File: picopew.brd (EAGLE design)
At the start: 48.4 x 20 mm, 16 parts, among them U1 IS31FL3733-TQLS4

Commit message: Silkscreen labeling and decorations.
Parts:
- added U$1: (no value), cwlogo:PICOPEW-O
- added U$10: (no value), cwtypeset:CHAR079
- added U$11: (no value), cwtypeset:CHAR078
- added U$12: (no value), cwlogo:MINUS
- added U$14, U$20, U$22: (no value), cwtypeset:CHAR082
- added U$15, U$21: (no value), cwtypeset:CHAR050
- added U$16: (no value), cwtypeset:CHAR048
- added U$17, U$19, U$25, U$26, U$9: (no value), cwtypeset:CHAR049
- added U$18, U$31: (no value), cwtypeset:CHAR057
- added U$2: (no value), cwlogo:PICOPEW-CORNER-L
- added U$23, U$29: (no value), cwtypeset:CHAR051
- added U$24: (no value), cwtypeset:CHAR067
- added U$27, U$30: (no value), cwtypeset:CHAR054
- added U$28: (no value), cwtypeset:CHAR055
- added U$3: (no value), cwlogo:PICOPEW-X
- added U$4: (no value), cwlogo:PLUS
- added U$5: (no value), cwlogo:PICOPEW
- added U$52, U$59: (no value), cwtypeset:CHAR104
- added U$53, U$54, U$77: (no value), cwtypeset:CHAR116
- added U$55, U$71: (no value), cwtypeset:CHAR112
- added U$56: (no value), cwtypeset:CHAR058
- added U$57, U$58, U$70, U$78: (no value), cwtypeset:CHAR047
- added U$6, U$72: (no value), cwtypeset:CHAR114
- added U$60, U$63, U$65: (no value), cwtypeset:CHAR097
- added U$61, U$76: (no value), cwtypeset:CHAR099
- added U$62: (no value), cwtypeset:CHAR107
- added U$64: (no value), cwtypeset:CHAR100
- added U$66: (no value), cwtypeset:CHAR121
- added U$67: (no value), cwtypeset:CHAR046
- added U$68: (no value), cwtypeset:CHAR105
- added U$69, U$73: (no value), cwtypeset:CHAR111
- added U$7: (no value), cwlogo:CWLOGO-4
- added U$74: (no value), cwtypeset:CHAR106
- added U$75: (no value), cwtypeset:CHAR101
- added U$8: (no value), cwlogo:PICOPEW-CORNER-R
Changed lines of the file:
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@@
 <element name="4" library="cwpackage" package="SINGLEPAD" value="SINGLEPAD" x="8" y="13.81"/>
 <element name="5" library="cwpackage" package="SINGLEPAD" value="SINGLEPAD" x="8" y="6.19"/>
+<element name="U$5" library="cwlogo" package="PICOPEW" value="" x="15.4" y="13.6" rot="R330"/>
+<element name="U$7" library="cwlogo" package="CWLOGO-4" value="" x="16.4" y="5.6" rot="R330"/>
+<element name="U$2" library="cwlogo" package="PICOPEW-CORNER-L" value="" x="2.4" y="0"/>
+<element name="U$8" library="cwlogo" package="PICOPEW-CORNER-R" value="" x="50.8" y="0"/>
+<element name="U$15" library="cwtypeset" package="CHAR050" value="" x="5.545896875" y="2.3" rot="R330"/>
+<element name="U$16" library="cwtypeset" package="CHAR048" value="" x="6.20840625" y="1.917503125" rot="R330"/>
+<element name="U$17" library="cwtypeset" package="CHAR049" value="" x="6.870915625" y="1.535003125" rot="R330"/>
+<element name="U$18" library="cwtypeset" package="CHAR057" value="" x="7.533425" y="1.152503125" rot="R330"/>
+<element name="U$6" library="cwtypeset" package="CHAR114" value="" x="12.941153125" y="12.92320625" rot="R330"/>
+<element name="U$9" library="cwtypeset" package="CHAR049" value="" x="13.382825" y="12.66820625" rot="R330"/>
+<element name="U$10" library="cwtypeset" package="CHAR079" value="" x="2.76435625" y="16.842821875" rot="R330"/>
+<element name="U$11" library="cwtypeset" package="CHAR078" value="" x="3.6373125" y="16.338821875" rot="R330"/>
+<element name="U$14" library="cwtypeset" package="CHAR082" value="" x="45.75" y="18.45" rot="MR270"/>
+<element name="U$19" library="cwtypeset" package="CHAR049" value="" x="45.75" y="17.625" rot="MR270"/>
+<element name="U$20" library="cwtypeset" package="CHAR082" value="" x="25.24" y="9.65"/>
+<element name="U$21" library="cwtypeset" package="CHAR050" value="" x="26.065" y="9.65"/>
+<element name="U$22" library="cwtypeset" package="CHAR082" value="" x="23.03" y="9.65"/>
+<element name="U$23" library="cwtypeset" package="CHAR051" value="" x="23.855" y="9.65"/>
+<element name="U$24" library="cwtypeset" package="CHAR067" value="" x="32.22" y="6.8"/>
+<element name="U$25" library="cwtypeset" package="CHAR049" value="" x="33.059" y="6.8"/>
+<element name="U$1" library="cwlogo" package="PICOPEW-O" value="" x="44.59" y="16.21" rot="R30"/>
+<element name="U$3" library="cwlogo" package="PICOPEW-X" value="" x="42.05" y="8.59" rot="R30"/>
+<element name="U$52" library="cwtypeset" package="CHAR104" value="" x="18.2" y="15.85" rot="MR270"/>
+<element name="U$53" library="cwtypeset" package="CHAR116" value="" x="18.2" y="15.036" rot="MR270"/>
+<element name="U$54" library="cwtypeset" package="CHAR116" value="" x="18.2" y="14.546" rot="MR270"/>
+<element name="U$55" library="cwtypeset" package="CHAR112" value="" x="18.2" y="14.056" rot="MR270"/>
+<element name="U$56" library="cwtypeset" package="CHAR058" value="" x="18.2" y="13.225" rot="MR270"/>
+<element name="U$57" library="cwtypeset" package="CHAR047" value="" x="18.2" y="12.894" rot="MR270"/>
+<element name="U$58" library="cwtypeset" package="CHAR047" value="" x="18.2" y="12.459" rot="MR270"/>
+<element name="U$59" library="cwtypeset" package="CHAR104" value="" x="18.2" y="12.024" rot="MR270"/>
+<element name="U$60" library="cwtypeset" package="CHAR097" value="" x="18.2" y="11.21" rot="MR270"/>
+<element name="U$61" library="cwtypeset" package="CHAR099" value="" x="18.2" y="10.483" rot="MR270"/>
+<element name="U$62" library="cwtypeset" package="CHAR107" value="" x="18.2" y="9.869" rot="MR270"/>
+<element name="U$63" library="cwtypeset" package="CHAR097" value="" x="18.2" y="9.119" rot="MR270"/>
+<element name="U$64" library="cwtypeset" package="CHAR100" value="" x="18.2" y="8.392" rot="MR270"/>
+<element name="U$65" library="cwtypeset" package="CHAR097" value="" x="18.2" y="7.564" rot="MR270"/>
+<element name="U$66" library="cwtypeset" package="CHAR121" value="" x="18.2" y="6.837" rot="MR270"/>
+<element name="U$67" library="cwtypeset" package="CHAR046" value="" x="18.2" y="6.116" rot="MR270"/>
+<element name="U$68" library="cwtypeset" package="CHAR105" value="" x="18.2" y="5.785" rot="MR270"/>
+<element name="U$69" library="cwtypeset" package="CHAR111" value="" x="18.2" y="5.434" rot="MR270"/>
+<element name="U$70" library="cwtypeset" package="CHAR047" value="" x="18.2" y="4.635" rot="MR270"/>
+<element name="U$71" library="cwtypeset" package="CHAR112" value="" x="20" y="14.7" rot="MR270"/>
+<element name="U$72" library="cwtypeset" package="CHAR114" value="" x="20" y="13.869" rot="MR270"/>
+<element name="U$73" library="cwtypeset" package="CHAR111" value="" x="20" y="13.359" rot="MR270"/>
+<element name="U$74" library="cwtypeset" package="CHAR106" value="" x="20" y="12.56" rot="MR270"/>
+<element name="U$75" library="cwtypeset" package="CHAR101" value="" x="20" y="12.183" rot="MR270"/>
+<element name="U$76" library="cwtypeset" package="CHAR099" value="" x="20" y="11.456" rot="MR270"/>
+<element name="U$77" library="cwtypeset" package="CHAR116" value="" x="20" y="10.842" rot="MR270"/>
+<element name="U$78" library="cwtypeset" package="CHAR047" value="" x="20" y="10.352" rot="MR270"/>
+<element name="U$26" library="cwtypeset" package="CHAR049" value="" x="20" y="9.917" rot="MR270"/>
+<element name="U$27" library="cwtypeset" package="CHAR054" value="" x="20" y="9.152" rot="MR270"/>
+<element name="U$28" library="cwtypeset" package="CHAR055" value="" x="20" y="8.387" rot="MR270"/>
+<element name="U$29" library="cwtypeset" package="CHAR051" value="" x="20" y="7.622" rot="MR270"/>
+<element name="U$30" library="cwtypeset" package="CHAR054" value="" x="20" y="6.857" rot="MR270"/>
+<element name="U$31" library="cwtypeset" package="CHAR057" value="" x="20" y="6.092" rot="MR270"/>
+<element name="U$4" library="cwlogo" package="PLUS" value="" x="8" y="11.8" rot="MR270"/>
+<element name="U$12" library="cwlogo" package="MINUS" value="" x="8" y="8.2" rot="MR270"/>
 </elements>
 <signals>

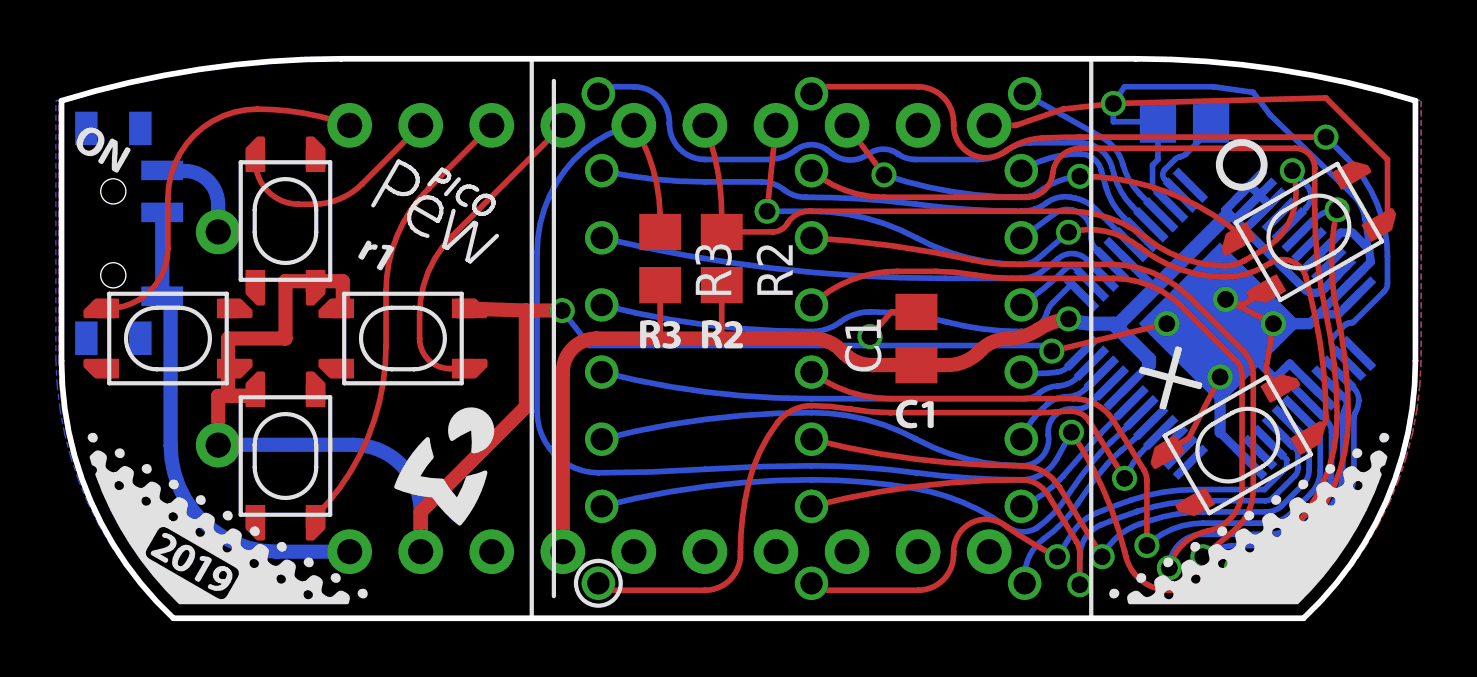
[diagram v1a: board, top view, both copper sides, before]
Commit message: Larger drill for the headers and smaller vias.
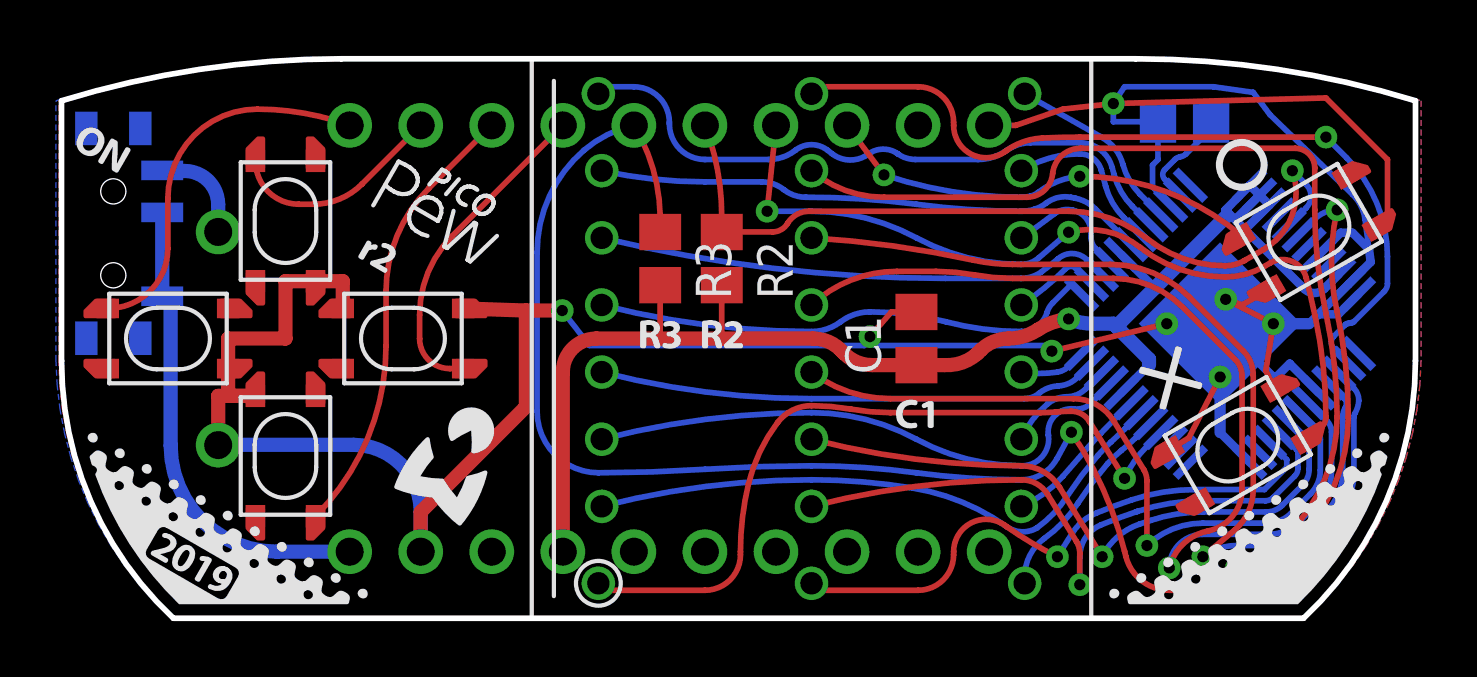
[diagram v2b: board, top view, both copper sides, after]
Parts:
- U$9: device cwtypeset:CHAR049 -> cwtypeset:CHAR050
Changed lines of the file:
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@@
 <element name="U$18" library="cwtypeset" package="CHAR057" value="" x="7.533425" y="1.152503125" rot="R330"/>
 <element name="U$6" library="cwtypeset" package="CHAR114" value="" x="12.941153125" y="12.92320625" rot="R330"/>
-<element name="U$9" library="cwtypeset" package="CHAR049" value="" x="13.382825" y="12.66820625" rot="R330"/>
+<element name="U$9" library="cwtypeset" package="CHAR050" value="" x="13.382825" y="12.66820625" rot="R330"/>
 <element name="U$10" library="cwtypeset" package="CHAR079" value="" x="2.76435625" y="16.842821875" rot="R330"/>
 <element name="U$11" library="cwtypeset" package="CHAR078" value="" x="3.6373125" y="16.338821875" rot="R330"/>
@@
 <wire x1="45.66554375" y1="11.804021875" x2="44.6" y2="11.2" width="0.2032" layer="1"/>
 <wire x1="44.6" y1="11.2" x2="44.015" y2="11.4" width="0.2032" layer="1"/>
-<via x="44.015" y="11.4" extent="1-16" drill="0.6"/>
+<via x="44.015" y="11.4" extent="1-16" drill="0.4" diameter="0.8128"/>
 <wire x1="44.015" y1="11.4" x2="43.815" y2="10.53" width="0.2032" layer="16"/>
-<via x="20.3" y="11" extent="1-16" drill="0.6"/>
+<via x="20.3" y="11" extent="1-16" drill="0.4" diameter="0.8128"/>
 <wire x1="20.3" y1="11" x2="21.2725" y2="9.75" width="0.2032" layer="16"/>
-<via x="37.8" y="9.55" extent="1-16" drill="0.6"/>
+<via x="37.8" y="9.55" extent="1-16" drill="0.4" diameter="0.8128"/>
 <wire x1="37.8" y1="9.55" x2="41.91" y2="10.53" width="0.2032" layer="1"/>
-<via x="41.91" y="10.53" extent="1-16" drill="0.6"/>
+<via x="41.91" y="10.53" extent="1-16" drill="0.4" diameter="0.8128"/>
 <wire x1="41.91" y1="10.53" x2="43.815" y2="10.53" width="0.2032" layer="16"/>
 <wire x1="35.56" y1="17.62" x2="36.5125" y2="17.62" width="0.2032" layer="1"/>
 <wire x1="36.5125" y1="17.62" x2="38.2" y2="18.2" width="0.2032" layer="1"/>
 <wire x1="38.2" y1="18.2" x2="40" y2="18.4" width="0.2032" layer="1"/>
-<via x="40" y="18.4" extent="1-16" drill="0.6"/>
-<via x="43.815" y="8.625" extent="1-16" drill="0.6"/>
+<via x="40" y="18.4" extent="1-16" drill="0.4" diameter="0.8128"/>
+<via x="43.815" y="8.625" extent="1-16" drill="0.4" diameter="0.8128"/>
 <wire x1="43.815" y1="6.6409125" x2="43.815" y2="10.53" width="0.4064" layer="16"/>
 <wire x1="44.015" y1="11.4" x2="45.72" y2="10.53" width="0.2032" layer="1"/>
-<via x="45.72" y="10.53" extent="1-16" drill="0.6"/>
+<via x="45.72" y="10.53" extent="1-16" drill="0.4" diameter="0.8128"/>
 <wire x1="45.72" y1="10.53" x2="43.815" y2="10.53" width="0.2032" layer="16"/>
 <contactref element="5" pad="1"/>
@@
 <wire x1="21.2725" y1="9.75" x2="31.1" y2="9.75" width="0.2032" layer="16"/>
 <wire x1="31.1" y1="9.75" x2="31.3" y2="10.0675" width="0.2032" layer="16"/>
-<via x="31.3" y="10.0675" extent="1-16" drill="0.6"/>
+<via x="31.3" y="10.0675" extent="1-16" drill="0.4" diameter="0.8128"/>
 <wire x1="31.3" y1="10.0675" x2="31.5" y2="9.75" width="0.2032" layer="16"/>
 <wire x1="32.96" y1="10.95" x2="32.065" y2="10.95" width="0.2032" layer="1"/>
@@
 <contactref element="U1" pad="2"/>
 <contactref element="1" pad="16"/>
-<via x="47.6" y="17.2" extent="1-16" drill="0.6"/>
+<via x="47.6" y="17.2" extent="1-16" drill="0.4" diameter="0.8128"/>
 <wire x1="36.192884375" y1="16.72845625" x2="36.11848125" y2="16.675640625" width="0.2032" layer="1"/>
 <wire x1="36.11848125" y1="16.675640625" x2="34.29" y2="17.61999375" width="0.2032" layer="1" curve="-125.370084"/>
@@
 <contactref element="U1" pad="3"/>
 <contactref element="1" pad="15"/>
-<via x="44.4" y="1.8" extent="1-16" drill="0.6"/>
+<via x="44.4" y="1.8" extent="1-16" drill="0.4" diameter="0.8128"/>
 <wire x1="37.829659375" y1="15.89285625" x2="36.90229375" y2="15.05" width="0.2032" layer="1" curve="-84.533565"/>
 <wire x1="36.90229375" y1="15.05" x2="31.8" y2="15.05" width="0.2032" layer="1"/>
@@
 <contactref element="U1" pad="4"/>
 <contactref element="1" pad="14"/>
-<via x="43.2" y="2.2" extent="1-16" drill="0.6"/>
+<via x="43.2" y="2.2" extent="1-16" drill="0.4" diameter="0.8128"/>
 <wire x1="47.7040875" y1="8.408678125" x2="48.25" y2="7.862765625" width="0.2032" layer="16"/>
 <wire x1="48.2" y1="7.2" x2="48.2" y2="5.228428125" width="0.2032" layer="16"/>
@@
 <contactref element="U1" pad="6"/>
 <contactref element="1" pad="13"/>
-<via x="42" y="1.8" extent="1-16" drill="0.6"/>
+<via x="42" y="1.8" extent="1-16" drill="0.4" diameter="0.8128"/>
 <wire x1="33.66" y1="12.4" x2="32.26" y2="12.4" width="0.2032" layer="1"/>
 <wire x1="46.99698125" y1="7.701571875" x2="47.624265625" y2="7.0742875" width="0.2032" layer="16"/>
@@
 <contactref element="U1" pad="7"/>
 <contactref element="1" pad="12"/>
-<via x="41.2" y="2.6" extent="1-16" drill="0.6"/>
+<via x="41.2" y="2.6" extent="1-16" drill="0.4" diameter="0.8128"/>
 <wire x1="46.643428125" y1="7.34801875" x2="47.268196875" y2="6.72325" width="0.2032" layer="16"/>
 <wire x1="47.268196875" y1="6.72325" x2="47.4" y2="6.40505" width="0.2032" layer="16" curve="-45.000398"/>
@@
 <contactref element="U1" pad="8"/>
 <contactref element="1" pad="11"/>
-<via x="39.6" y="2.2" extent="1-16" drill="0.6"/>
+<via x="39.6" y="2.2" extent="1-16" drill="0.4" diameter="0.8128"/>
 <wire x1="47" y1="5.331371875" x2="47" y2="6.160075" width="0.2032" layer="16"/>
 <wire x1="47" y1="6.160075" x2="46.91213125" y2="6.372209375" width="0.2032" layer="16" curve="45.000422"/>
@@
 <contactref element="U1" pad="9"/>
 <contactref element="1" pad="10"/>
-<via x="38.8" y="1.2" extent="1-16" drill="0.6"/>
+<via x="38.8" y="1.2" extent="1-16" drill="0.4" diameter="0.8128"/>
 <wire x1="46.6" y1="5.365684375" x2="46.6" y2="5.915103125" width="0.2032" layer="16"/>
 <wire x1="46.6" y1="5.915103125" x2="46.556065625" y2="6.02116875" width="0.2032" layer="16" curve="45"/>
@@
 <contactref element="U1" pad="10"/>
 <contactref element="1" pad="9"/>
-<via x="38" y="2.2" extent="1-16" drill="0.6"/>
+<via x="38" y="2.2" extent="1-16" drill="0.4" diameter="0.8128"/>
 <wire x1="36.192884375" y1="3.27154375" x2="36.118484375" y2="3.324359375" width="0.2032" layer="1"/>
 <wire x1="36.118484375" y1="3.324359375" x2="34.29" y2="2.38" width="0.2032" layer="1" curve="125.370031"/>
@@
 <wire x1="26.67" y1="2.27" x2="25.4" y2="1" width="0.2032" layer="1" curve="-90"/>
 <wire x1="25.4" y1="1" x2="21.84" y2="1" width="0.2032" layer="1"/>
-<via x="40.4" y="5" extent="1-16" drill="0.6"/>
+<via x="40.4" y="5" extent="1-16" drill="0.4" diameter="0.8128"/>
 <wire x1="41.69368125" y1="6.6409125" x2="41.2" y2="6.14723125" width="0.2032" layer="16"/>
 <wire x1="37.4" y1="7.35" x2="32.0325" y2="7.35" width="0.2032" layer="1"/>
@@
 <wire x1="46.88790625" y1="14.6635625" x2="46.88790625" y2="15.51209375" width="0.2032" layer="16" curve="90"/>
 <wire x1="46.88790625" y1="15.51209375" x2="46.4" y2="16" width="0.2032" layer="16"/>
-<via x="46.4" y="16" extent="1-16" drill="0.6"/>
+<via x="46.4" y="16" extent="1-16" drill="0.4" diameter="0.8128"/>
 <wire x1="28.35189375" y1="14.1135125" x2="29.121775" y2="14.55" width="0.2032" layer="1" curve="-59.102503"/>
 <wire x1="29.121775" y1="14.55" x2="38.4" y2="14.55" width="0.2032" layer="1"/>
@@
 <contactref element="U1" pad="42"/>
 <contactref element="R3" pad="1"/>
-<via x="38.5" y="6.65" extent="1-16" drill="0.6"/>
-<via x="48" y="14.6" extent="1-16" drill="0.6"/>
+<via x="38.5" y="6.65" extent="1-16" drill="0.4" diameter="0.8128"/>
+<via x="48" y="14.6" extent="1-16" drill="0.4" diameter="0.8128"/>
 <wire x1="40.4" y1="2.4" x2="40.447015625" y2="2.2119375" width="0.2032" layer="1"/>
 <wire x1="40.447015625" y1="2.2119375" x2="41.99924375" y2="1" width="0.2032" layer="1" curve="75.963784"/>
@@
 <wire x1="21.52" y1="10" x2="23.8" y2="10" width="0.508" layer="1"/>
 <wire x1="23.8" y1="10" x2="26" y2="10" width="0.508" layer="1"/>
-<via x="38.4" y="10.7" extent="1-16" drill="0.6"/>
+<via x="38.4" y="10.7" extent="1-16" drill="0.4" diameter="0.8128"/>
 <wire x1="26" y1="11.9075" x2="26" y2="10" width="0.2032" layer="1"/>
 <wire x1="23.8" y1="11.9075" x2="23.8" y2="10" width="0.2032" layer="1"/>
@@
 <contactref element="O" pad="1"/>
 <wire x1="30.48" y1="17.62" x2="31.8" y2="15.85" width="0.2032" layer="1"/>
-<via x="31.8" y="15.85" extent="1-16" drill="0.6"/>
-<via x="38.8" y="15.8" extent="1-16" drill="0.6"/>
+<via x="31.8" y="15.85" extent="1-16" drill="0.4" diameter="0.8128"/>
+<via x="38.8" y="15.8" extent="1-16" drill="0.4" diameter="0.8128"/>
 <contactref element="O" pad="2"/>
 <wire x1="38.8" y1="15.8" x2="44.59054375" y2="13.665975" width="0.2032" layer="1" curve="-40.461333"/>
@@
 </signal>
 <signal name="N$29">
-<via x="38.4" y="13.8" extent="1-16" drill="0.6"/>
+<via x="38.4" y="13.8" extent="1-16" drill="0.4" diameter="0.8128"/>
 <contactref element="2" pad="32"/>
 <wire x1="27.94" y1="17.62" x2="27.6225" y2="14.55" width="0.2032" layer="1"/>
-<via x="27.6225" y="14.55" extent="1-16" drill="0.6"/>
+<via x="27.6225" y="14.55" extent="1-16" drill="0.4" diameter="0.8128"/>
 <wire x1="27.6225" y1="14.55" x2="29.21" y2="14.55" width="0.2032" layer="16"/>
 <contactref element="X" pad="3"/>
